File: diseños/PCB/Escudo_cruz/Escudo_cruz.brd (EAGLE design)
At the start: 100 x 80 mm, 12 parts, among them X1 TERMINAL-BLOCK-3.5MM-3-PIN-RO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, X2 TERMINAL-BLOCK-3.5MM-3-PIN-RO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, X3 TERMINAL-BLOCK-3.5MM-3-PIN-RO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, X4 TERMINAL-BLOCK-3.5MM-3-PIN-RO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

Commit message: Cortes Mes y Año
Grupo tres capa 1 y 3
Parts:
- added SW1: (no value), adafruit:PUSHBUTTON_SMD_SJ
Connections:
- new net N$5: SW1.P$1, U$3.RST
- net GND: now also SW1.P$2
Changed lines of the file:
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@@
 <attribute name="VALUE" x="86" y="18.254" size="0.0254" layer="27"/>
+</element>
+<element name="SW1" library="adafruit" library_urn="urn:adsk.eagle:library:420" package="PUSHBUTTON_SMD_SJ" package3d_urn="urn:adsk.eagle:package:6240956/1" value="" x="86.36" y="40.64" smashed="yes">
+<attribute name="NAME" x="84.582" y="40.767" size="0.8128" layer="25" ratio="18"/>
+<attribute name="VALUE" x="84.582" y="39.878" size="0.4064" layer="27" ratio="10"/>
 </element>
 </elements>
@@
 <contactref element="X4" pad="3"/>
 <contactref element="GND" pad="MP"/>
+<contactref element="SW1" pad="P$2"/>
 <wire x1="51.76" y1="41.81" x2="74.93" y2="36.83" width="0" layer="19" extent="1-1"/>
 <wire x1="37.79" y1="41.81" x2="51.76" y2="41.81" width="0" layer="19" extent="1-1"/>
@@
 <wire x1="8.34" y1="23.44" x2="9.85" y2="41.81" width="0" layer="19" extent="1-1"/>
 <wire x1="52.07" y1="15.24" x2="51.76" y2="41.81" width="0" layer="19" extent="1-1"/>
-<wire x1="86" y1="3" x2="8.34" y2="23.44" width="0" layer="19" extent="1-1"/>
+<wire x1="83.36" y1="40.64" x2="8.34" y2="23.44" width="0" layer="19" extent="1-1"/>
+<wire x1="86" y1="3" x2="74.93" y2="36.83" width="0" layer="19" extent="1-1"/>
 </signal>
 <signal name="GND@1">
@@
 <wire x1="8.37" y1="29.04" x2="22.34" y2="23.44" width="0" layer="19" extent="1-1"/>
 </signal>
+<signal name="N$5">
+<contactref element="U$3" pad="RST"/>
+<contactref element="SW1" pad="P$1"/>
+<wire x1="89.36" y1="40.64" x2="29.21" y2="7.62" width="0" layer="19" extent="1-1"/>
+</signal>
 </signals>

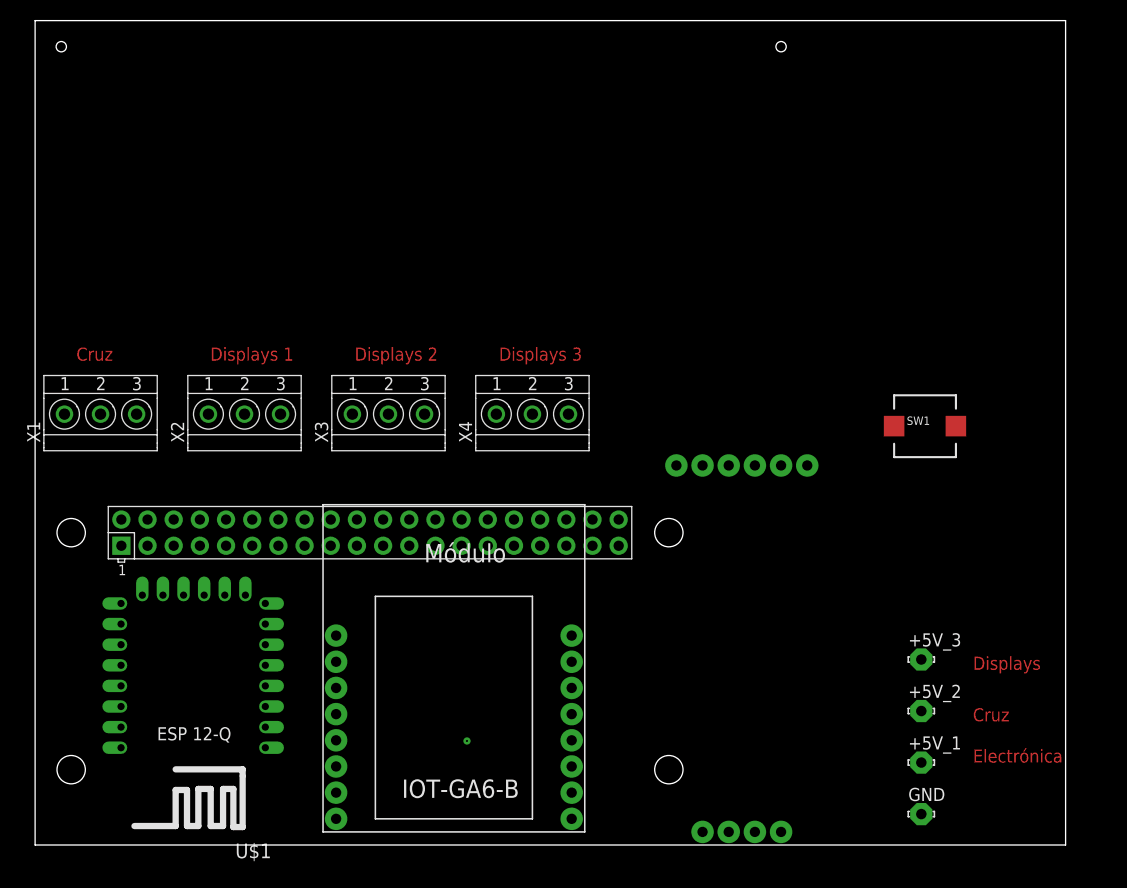
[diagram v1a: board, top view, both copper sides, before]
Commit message: Modificaciones SHIELD raspberry
Se descarta la idea de la comunicación I2C y se agrega una quinta salida de display para indicar la tonalidad del tipo de accidente.
Cambios a los cortes del grupo 2 capas 1, 2 y 3
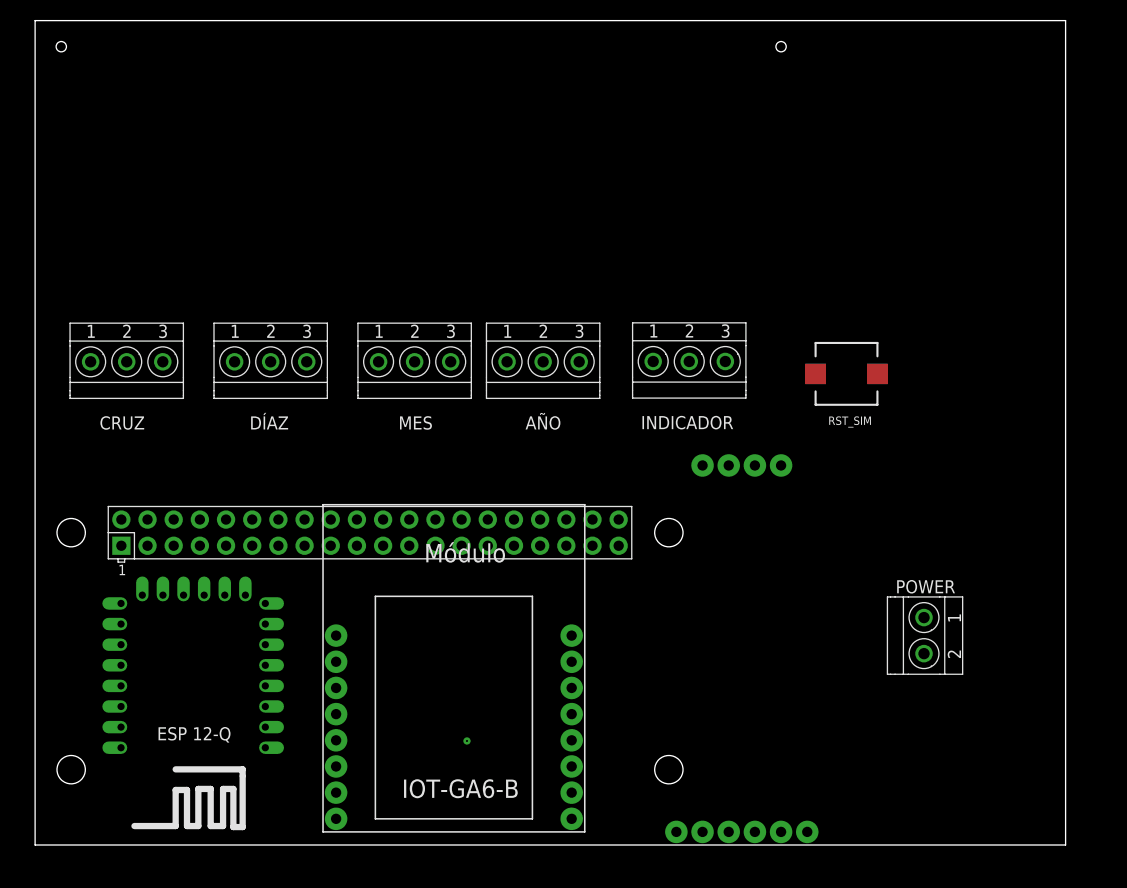
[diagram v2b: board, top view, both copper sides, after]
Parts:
- removed +5V_1, +5V_2, +5V_3, GND: LSP10, solpad:LSP10
- removed SW1: (no value), adafruit:PUSHBUTTON_SMD_SJ
- removed X1, X2, X3, X4: TERMINAL-BLOCK-3.5MM-3-PIN-ROUND-PAD, Rembrandt Electronics - Terminal Block 3-5mm v1-0:TERMINAL-BLOCK-3-PIN-3.5MM-ROUND-PAD
- added AÑO, CRUZ, DÍAZ, INDICADOR, MES: TERMINAL-BLOCK-3.5MM-3-PIN-ROUND-PAD, Rembrandt Electronics - Terminal Block 3-5mm v1-0:TERMINAL-BLOCK-3-PIN-3.5MM-ROUND-PAD
- added POWER: TERMINAL-BLOCK-3.5MM-2-PIN-ROUND-PAD, Rembrandt Electronics - Terminal Block 3-5mm v1-0:TERMINAL-BLOCK-2-PIN-3.5MM-ROUND-PAD
- added RST_SIM: (no value), adafruit:PUSHBUTTON_SMD_SJ
- moved U$4 38.1 mm to (68.6, 0.00), turned to 90 degrees
- renumbered U$1 to ESP8266, U$3 to SIM
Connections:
- removed net +5V_1: +5V_1.MP, SIM.VCC, U$2.2, U$4.VCC
- removed net +5V_2: +5V_2.MP, X1.2
- removed net +5V_3: +5V_3.MP, X2.2, X3.2, X4.2
- new net +5V: AÑO.2, CRUZ.2, DÍAZ.2, MES.2, POWER.1, SIM.VCC, U$2.2
- new net N$10: U$4.VCC2
- new net N$6: INDICADOR.2
- new net N$9: ESP8266.GPIO14, INDICADOR.1
- net GND: now also AÑO.3, CRUZ.3, DÍAZ.3, INDICADOR.3, MES.3, RST_SIM.P$2, U$4.GND2; no longer GND.MP, SW1.P$2, U$4.GND, X1.3, X2.3, X3.3, X4.3
- net N$12: now also DÍAZ.1; no longer X2.1
- net N$13: now also MES.1; no longer X3.1
- net N$14: now also AÑO.1; no longer X4.1
- net N$3: now also U$4.SDA2; no longer ESP8266.GPIO12, U$4.SDA
- net N$4: now also U$4.SCL2; no longer ESP8266.GPIO14, U$4.SCL
- net N$5: now also RST_SIM.P$1; no longer SW1.P$1
- net N$7: now also CRUZ.1; no longer X1.1
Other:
- board text removed: "Cruz"
- board text removed: "Displays"
- board text removed: "Displays 1"
- board text removed: "Displays 2"
- board text removed: "Displays 3"
- board text removed: "Electrónica"
